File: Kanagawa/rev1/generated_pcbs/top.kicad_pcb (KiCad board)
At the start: 2 copper layers, 330 x 142 mm, 7 parts

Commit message: edit arc for edge cut in script
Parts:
- removed MountBaseMiddleTop7: MountingHole, keyboard:MountingHole_2.2mm_M2_Pad_Via
- moved MountBaseMiddleTop1 2.40 mm to (60.0, 81.0)
- moved MountBaseMiddleTop5 2.23 mm to (381.0, 81.0)
- moved MountBaseMiddleTop3 2.00 mm to (244.9, 81.2)
- moved MountBaseMiddleTop2 0.92 mm to (60.0, 207.0)
- moved MountBaseMiddleTop4 0.92 mm to (244.0, 207.0)
- moved MountBaseMiddleTop6 0.92 mm to (380.0, 207.0)
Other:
- board size 330 x 142 mm -> 330 x 144 mm

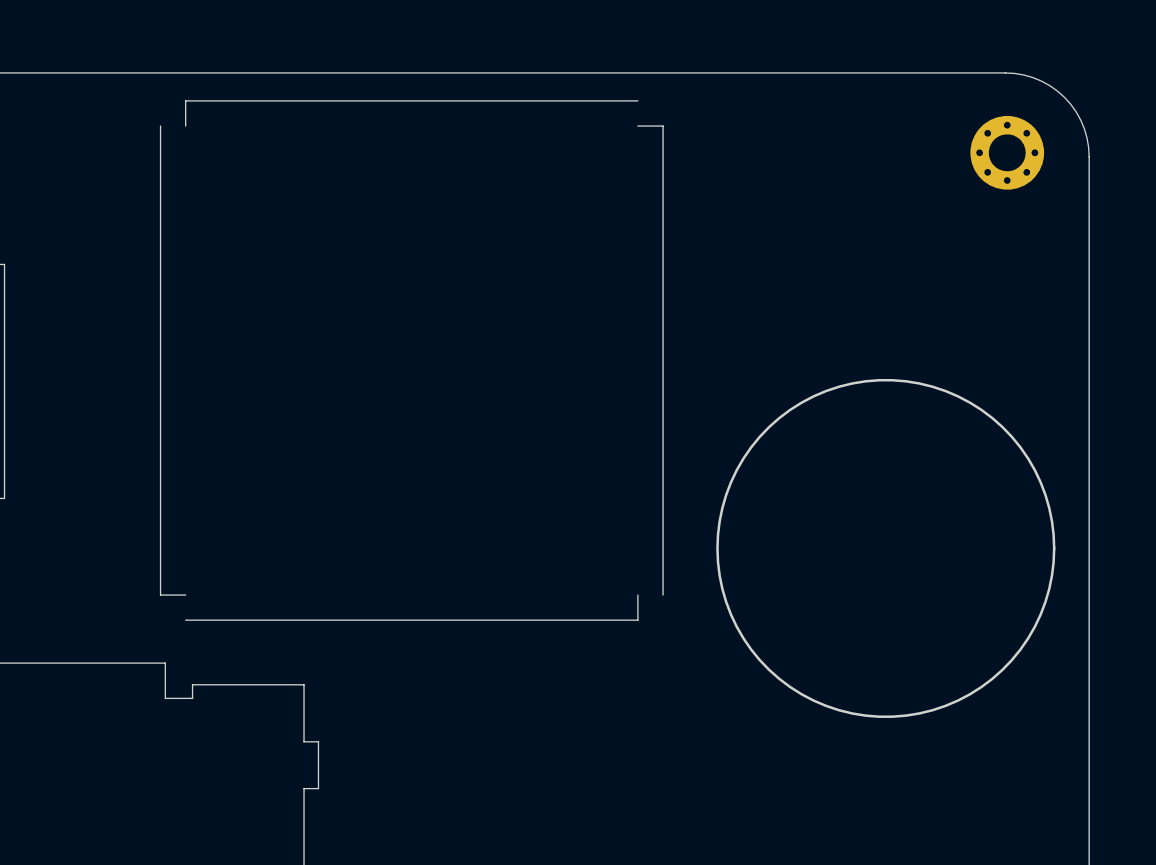
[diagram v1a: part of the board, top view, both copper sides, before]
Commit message: update script pcb generation
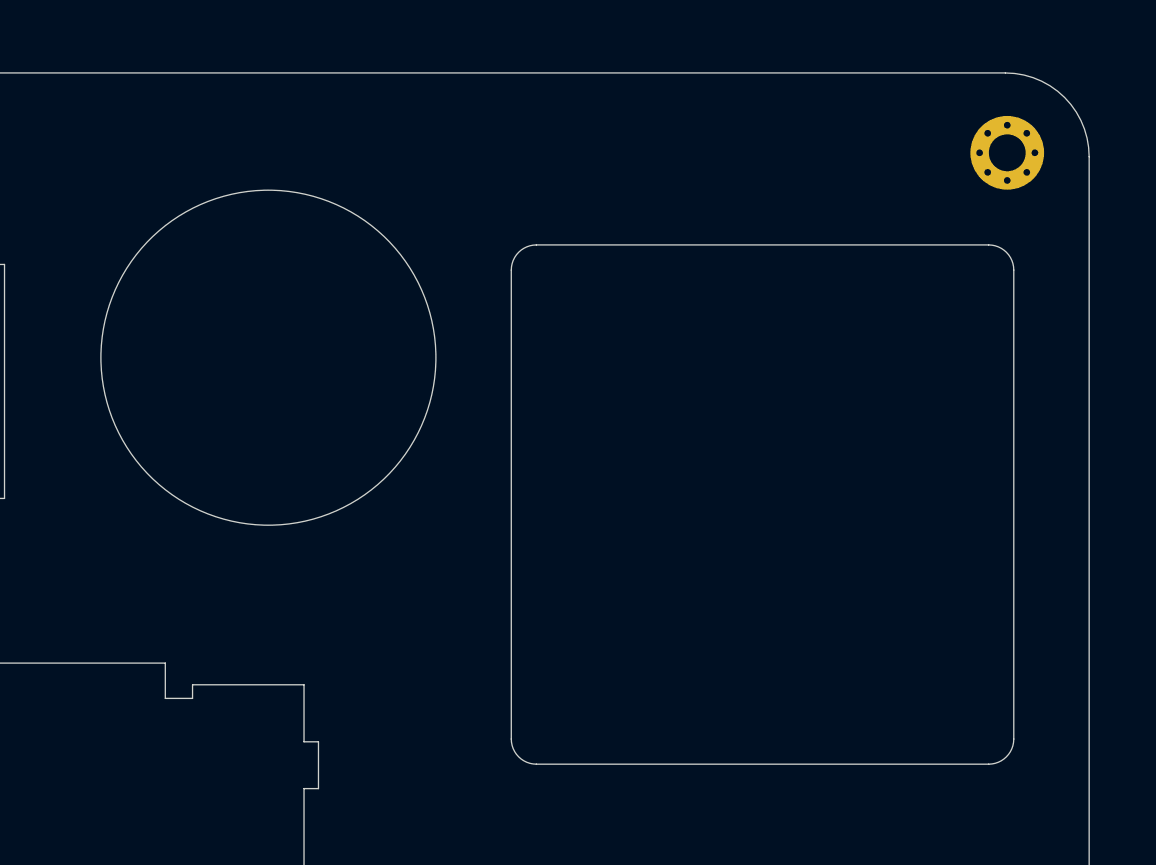
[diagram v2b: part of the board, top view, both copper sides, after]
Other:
- outline, holes or cut-outs redrawn

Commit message: rework rev1 from fusion layout
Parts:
- added MountBaseMiddleTop3: MountingHole, keyboard:MountingHole_2.2mm_M2_Pad_Via, F.Cu at (125.9, 81.2)
- added MountBaseMiddleTop4: MountingHole, keyboard:MountingHole_2.2mm_M2_Pad_Via, F.Cu at (125.9, 207.2)
- moved MountBaseMiddleTop7 4.12 mm to (376.9, 81.2)
- moved MountBaseMiddleTop8 3.12 mm to (376.9, 207.2)
- moved MountBaseMiddleTop1 1.90 mm to (61.9, 81.2)
- moved MountBaseMiddleTop2 1.90 mm to (61.9, 207.2)
- moved MountBaseMiddleTop6 0.92 mm to (244.9, 207.2)
- renumbered MountBaseMiddleTop3 to MountBaseMiddleTop5, MountBaseMiddleTop4 to MountBaseMiddleTop6, MountBaseMiddleTop5 to MountBaseMiddleTop7, MountBaseMiddleTop6 to MountBaseMiddleTop8
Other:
- board size 330 x 144 mm -> 325 x 146 mm

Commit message: review board
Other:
- board size 325 x 146 mm -> 325 x 145 mm

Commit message: generate kanagawa gerber
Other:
- board size 325 x 145 mm -> 325 x 143 mm

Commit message: re route pcbs
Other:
- board size 325 x 143 mm -> 325 x 145 mm
- net class Default removed

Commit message: release 1.0
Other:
- outline, holes or cut-outs redrawn
